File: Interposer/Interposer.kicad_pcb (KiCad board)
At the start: 2 copper layers, 55 x 52 mm, 34 parts, among them J7 Conn_01x14_MountingPin, Q3 2N7002, U13 AD40xxBRMZ, U14 LP5907MFX-1.8, U6 ADA4940-1xCP

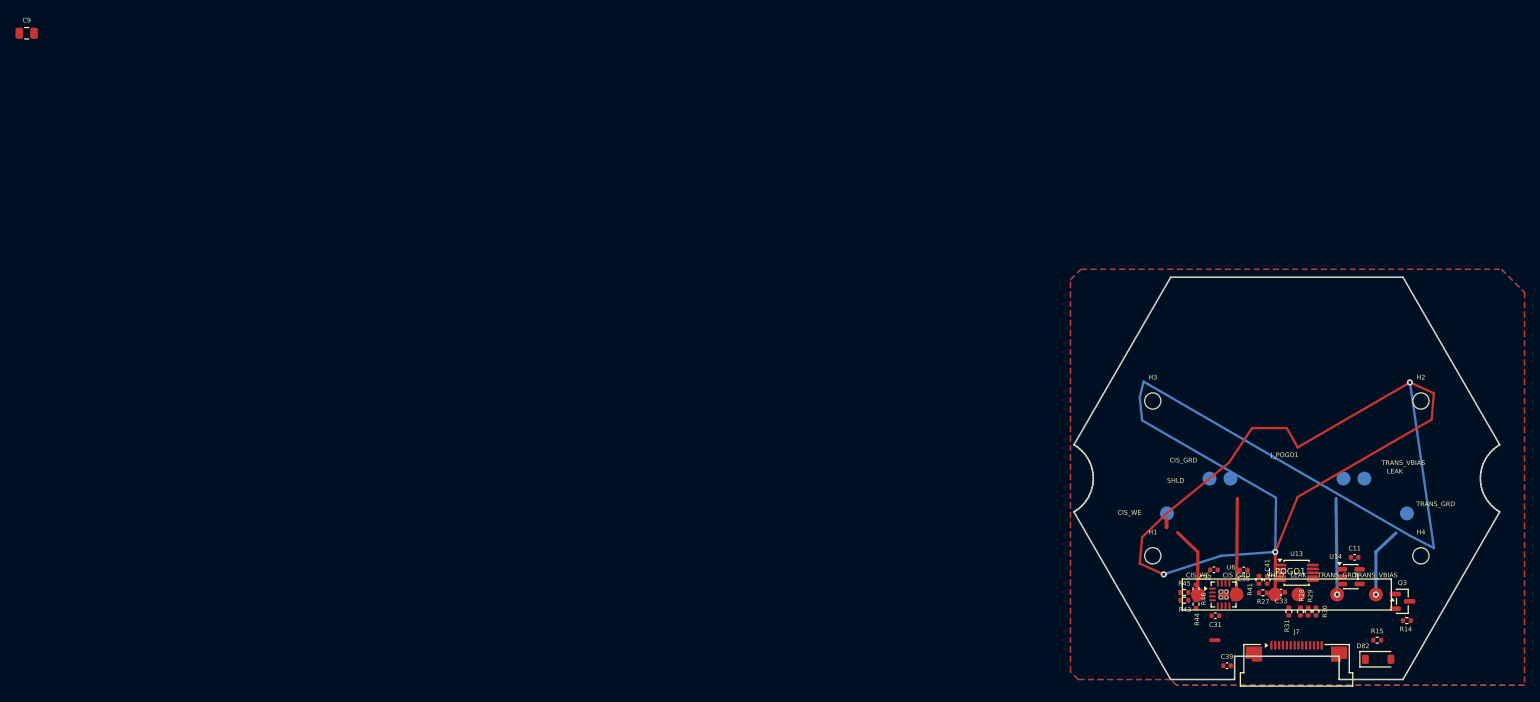
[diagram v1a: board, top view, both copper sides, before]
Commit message: fix(interposer): add missing H2-H4 holes and 12-pin pogo target array
Co-authored-by: google-labs-jules[bot] <161369871+google-labs-jules[bot]@users.noreply.github.com>
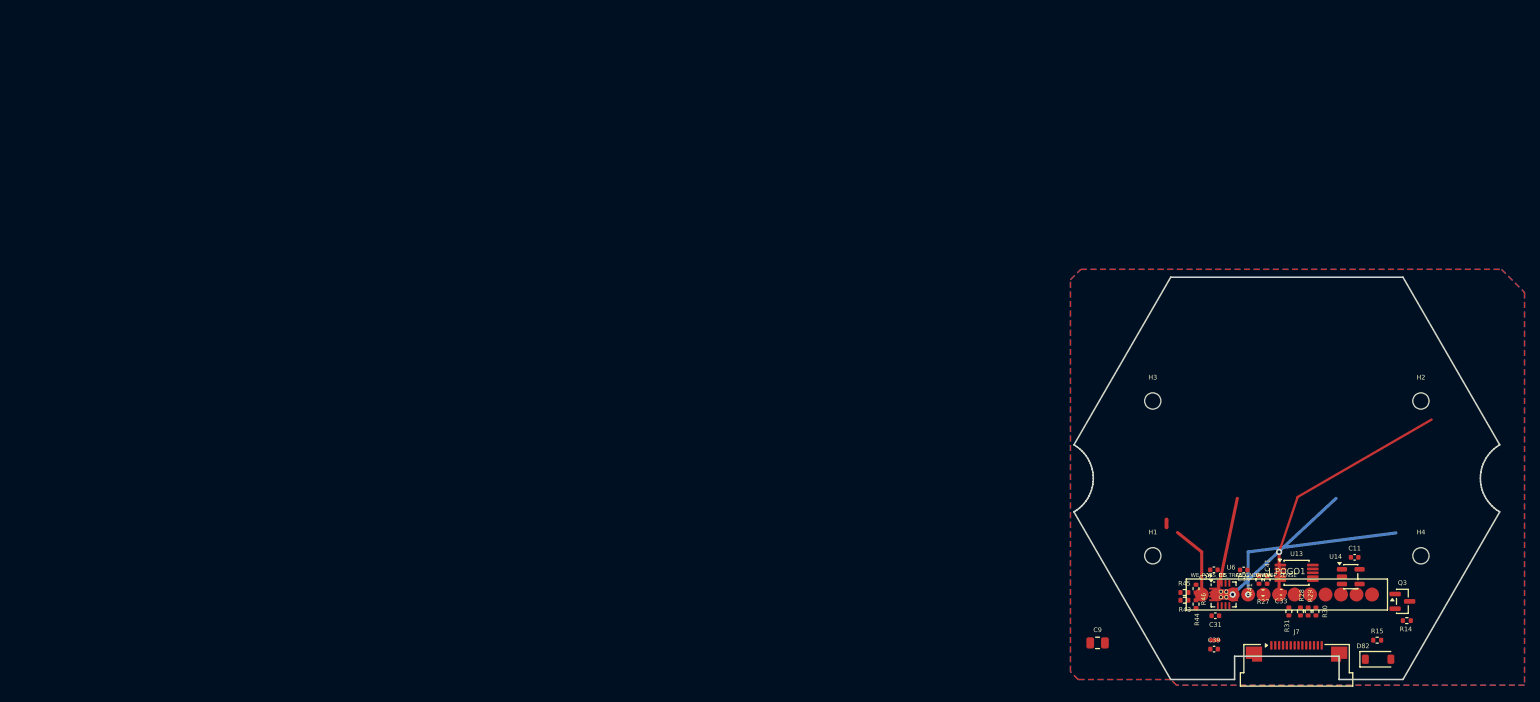
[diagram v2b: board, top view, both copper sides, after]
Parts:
- removed the J_POGO1 at (164.5, 58.5)
- moved C9 159.2 mm to (140.1, 79.8)
- moved C39 2.72 mm to (155.1, 80.5)
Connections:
- net /Signal_AMP renamed /Signal_Return
- J7 pad 10: VSSA -> VDDA
- J7 pad 12: VDDA -> VSSA
- J_POGO1 pad 1: >PORE_AMP -> WE_POS
- J_POGO1 pad 2: GUARD -> WS_CIS
- J_POGO1 pad 3: GNDA -> RE_TRANS
- J_POGO1 pad 4: WEEP_SENSE -> CE_GNDA
- J_POGO1 pad 5: GUARD_TRANS -> GNDA
- J_POGO1 pad 6: Vbias -> WEEP_SENSE
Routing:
- net WEEP_SENSE: track 202.8 -> 33.0 mm, vias 3 -> 1
- net CE_GNDA: track 9.07 -> 24.8 mm
- net RE_TRANS: track 12.4 -> 18.2 mm

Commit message: fix: Reconcile MR1 board stackup, BOM, interposer, and pore guidelines
Co-authored-by: google-labs-jules[bot] <161369871+google-labs-jules[bot]@users.noreply.github.com>
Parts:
- removed C11: 4.7u, Capacitor_SMD:C_0402_1005Metric
- removed C31, C32, C33, C39: 100nF, Capacitor_SMD:C_0402_1005Metric
- removed C35: 10u, Capacitor_SMD:C_0402_1005Metric
- removed C41: 1nF, Capacitor_SMD:C_0402_1005Metric
- removed C9: 100nF, Capacitor_SMD:C_0805_2012Metric
- removed D82: MBR0540, Diode_SMD:D_SOD-123
- removed J7: Conn_01x14_MountingPin, Connector_FFC-FPC:Amphenol_F32R-1A7x1-11014_1x14-1MP_P0.5mm_Horizontal
- removed NT7, NT8: NetTie_2, NetTie:NetTie-2_SMD_Pad0.5mm
- removed Q3: 2N7002, Package_TO_SOT_SMD:SOT-23
- removed R14, R15: 100k, Resistor_SMD:R_0402_1005Metric
- removed R27, R41: 27, Resistor_SMD:R_0402_1005Metric
- removed R28, R29, R30, R31: 49.9, Resistor_SMD:R_0402_1005Metric
- removed R43, R44, R45, R46: 499 (0.1%), Resistor_SMD:R_0402_1005Metric
- removed U13: AD40xxBRMZ, Package_SO:MSOP-10_3x3mm_P0.5mm
- removed U14: LP5907MFX-1.8, Package_TO_SOT_SMD:SOT-23-5
- removed U6: ADA4940-1xCP, Package_CSP:LFCSP-16-1EP_3x3mm_P0.5mm_EP1.3x1.3mm_ThermalVias

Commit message: feat: Add Path 2 wideband TIA channel for 200nm pores
Co-authored-by: google-labs-jules[bot] <161369871+google-labs-jules[bot]@users.noreply.github.com>
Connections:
- J_POGO1 pad 1: WE_POS -> CE_GNDA
- J_POGO1 pad 10: GUARD -> WS_CIS_WIDE
- J_POGO1 pad 11: GUARD -> GNDA
- J_POGO1 pad 12: GUARD -> WEEP_SENSE
- J_POGO1 pad 2: WS_CIS -> RE_TRANS
- J_POGO1 pad 3: RE_TRANS -> >PORE
- J_POGO1 pad 4: CE_GNDA -> GNDA
- J_POGO1 pad 5: GNDA -> GUARD
- J_POGO1 pad 6: WEEP_SENSE -> WS_CIS
- J_POGO1 pad 7: GUARD_TRANS -> GUARD
- J_POGO1 pad 8: GUARD -> GNDA
- J_POGO1 pad 9: GUARD -> GUARD_WIDE
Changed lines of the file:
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@@
 				(type "core")
 				(color "PTFE natural")
-				(thickness 0.71)
-				(material "PTFE")
+				(thickness 1.5)
+				(material "Rogers RO3003 / PTFE")
 				(epsilon_r 2.1)
 				(loss_tangent 0.0002)
@@
 		(fp_line (start 13.0 2.0) (end -13.0 2.0) (stroke (width 0.15) (type default)) (layer "F.SilkS"))
 		(fp_line (start -13.0 2.0) (end -13.0 -2.0) (stroke (width 0.15) (type default)) (layer "F.SilkS"))
-		(fp_text user "WE_POS" (at -11.0 -2.5 0) (layer "F.SilkS") (effects (font (size 0.5 0.5) (thickness 0.08))))
-		(fp_text user "WS_CIS" (at -9.0 -2.5 0) (layer "F.SilkS") (effects (font (size 0.5 0.5) (thickness 0.08))))
-		(fp_text user "RE_TRANS" (at -7.0 -2.5 0) (layer "F.SilkS") (effects (font (size 0.5 0.5) (thickness 0.08))))
-		(fp_text user "CE_GNDA" (at -5.0 -2.5 0) (layer "F.SilkS") (effects (font (size 0.5 0.5) (thickness 0.08))))
-		(fp_text user "GNDA" (at -3.0 -2.5 0) (layer "F.SilkS") (effects (font (size 0.5 0.5) (thickness 0.08))))
-		(fp_text user "WEEP_SENSE" (at -1.0 -2.5 0) (layer "F.SilkS") (effects (font (size 0.5 0.5) (thickness 0.08))))
-		(pad "1" smd circle (at -11.0 0) (size 1.8 1.8) (layers "F.Cu" "F.Mask") (clearance 0.4) (zone_connect 0) (net "WE_POS"))
-		(pad "2" smd circle (at -9.0 0) (size 1.8 1.8) (layers "F.Cu" "F.Mask") (clearance 0.4) (zone_connect 0) (net "WS_CIS"))
-		(pad "3" smd circle (at -7.0 0) (size 1.8 1.8) (layers "F.Cu" "F.Mask") (clearance 0.4) (zone_connect 0) (net "RE_TRANS"))
-		(pad "4" smd circle (at -5.0 0) (size 1.8 1.8) (layers "F.Cu" "F.Mask") (clearance 0.4) (zone_connect 0) (net "CE_GNDA"))
-		(pad "5" smd circle (at -3.0 0) (size 1.8 1.8) (layers "F.Cu" "F.Mask") (clearance 0.4) (zone_connect 0) (net "GNDA"))
-		(pad "6" smd circle (at -1.0 0) (size 1.8 1.8) (layers "F.Cu" "F.Mask") (clearance 0.4) (zone_connect 0) (net "WEEP_SENSE"))
-		(pad "7" smd circle (at 1.0 0) (size 1.8 1.8) (layers "F.Cu" "F.Mask") (clearance 0.4) (zone_connect 0) (net "GUARD_TRANS"))
-		(pad "8" smd circle (at 3.0 0) (size 1.8 1.8) (layers "F.Cu" "F.Mask") (clearance 0.4) (zone_connect 0) (net "GUARD"))
-		(pad "9" smd circle (at 5.0 0) (size 1.8 1.8) (layers "F.Cu" "F.Mask") (clearance 0.4) (zone_connect 0) (net "GUARD"))
-		(pad "10" smd circle (at 7.0 0) (size 1.8 1.8) (layers "F.Cu" "F.Mask") (clearance 0.4) (zone_connect 0) (net "GUARD"))
-		(pad "11" smd circle (at 9.0 0) (size 1.8 1.8) (layers "F.Cu" "F.Mask") (clearance 0.4) (zone_connect 0) (net "GUARD"))
-		(pad "12" smd circle (at 11.0 0) (size 1.8 1.8) (layers "F.Cu" "F.Mask") (clearance 0.4) (zone_connect 0) (net "GUARD"))
+		(fp_text user "CE_GNDA" (at -11.0 -2.5 0) (layer "F.SilkS") (uuid "uuid-1") (effects (font (size 0.5 0.5) (thickness 0.08))))
+		(fp_text user "RE_TRANS" (at -9.0 -2.5 0) (layer "F.SilkS") (uuid "uuid-2") (effects (font (size 0.5 0.5) (thickness 0.08))))
+		(fp_text user ">PORE" (at -7.0 -2.5 0) (layer "F.SilkS") (uuid "uuid-3") (effects (font (size 0.5 0.5) (thickness 0.08))))
+		(fp_text user "GNDA" (at -5.0 -2.5 0) (layer "F.SilkS") (uuid "uuid-4") (effects (font (size 0.5 0.5) (thickness 0.08))))
+		(fp_text user "GUARD" (at -3.0 -2.5 0) (layer "F.SilkS") (uuid "uuid-5") (effects (font (size 0.5 0.5) (thickness 0.08))))
+		(fp_text user "WS_CIS" (at -1.0 -2.5 0) (layer "F.SilkS") (uuid "uuid-6") (effects (font (size 0.5 0.5) (thickness 0.08))))
+		(fp_text user "GUARD" (at 1.0 -2.5 0) (layer "F.SilkS") (uuid "uuid-7") (effects (font (size 0.5 0.5) (thickness 0.08))))
+		(fp_text user "GNDA" (at 3.0 -2.5 0) (layer "F.SilkS") (uuid "uuid-8") (effects (font (size 0.5 0.5) (thickness 0.08))))
+		(fp_text user "GUARD_WIDE" (at 5.0 -2.5 0) (layer "F.SilkS") (uuid "uuid-9") (effects (font (size 0.5 0.5) (thickness 0.08))))
+		(fp_text user "WS_CIS_WIDE" (at 7.0 -2.5 0) (layer "F.SilkS") (uuid "uuid-10") (effects (font (size 0.5 0.5) (thickness 0.08))))
+		(fp_text user "GNDA" (at 9.0 -2.5 0) (layer "F.SilkS") (uuid "uuid-11") (effects (font (size 0.5 0.5) (thickness 0.08))))
+		(fp_text user "WEEP_SENSE" (at 11.0 -2.5 0) (layer "F.SilkS") (uuid "uuid-12") (effects (font (size 0.5 0.5) (thickness 0.08))))
+		(pad "1" smd circle (at -11.0 0) (size 1.8 1.8) (layers "F.Cu" "F.Mask") (clearance 0.4) (zone_connect 0) (net "CE_GNDA") (uuid "uuid-pad-1"))
+		(pad "2" smd circle (at -9.0 0) (size 1.8 1.8) (layers "F.Cu" "F.Mask") (clearance 0.4) (zone_connect 0) (net "RE_TRANS") (uuid "uuid-pad-2"))
+		(pad "3" smd circle (at -7.0 0) (size 1.8 1.8) (layers "F.Cu" "F.Mask") (clearance 0.4) (zone_connect 0) (net ">PORE") (uuid "uuid-pad-3"))
+		(pad "4" smd circle (at -5.0 0) (size 1.8 1.8) (layers "F.Cu" "F.Mask") (clearance 0.4) (zone_connect 0) (net "GNDA") (uuid "uuid-pad-4"))
+		(pad "5" smd circle (at -3.0 0) (size 1.8 1.8) (layers "F.Cu" "F.Mask") (clearance 0.4) (zone_connect 0) (net "GUARD") (uuid "uuid-pad-5"))
+		(pad "6" smd circle (at -1.0 0) (size 1.8 1.8) (layers "F.Cu" "F.Mask") (clearance 0.4) (zone_connect 0) (net "WS_CIS") (uuid "uuid-pad-6"))
+		(pad "7" smd circle (at 1.0 0) (size 1.8 1.8) (layers "F.Cu" "F.Mask") (clearance 0.4) (zone_connect 0) (net "GUARD") (uuid "uuid-pad-7"))
+		(pad "8" smd circle (at 3.0 0) (size 1.8 1.8) (layers "F.Cu" "F.Mask") (clearance 0.4) (zone_connect 0) (net "GNDA") (uuid "uuid-pad-8"))
+		(pad "9" smd circle (at 5.0 0) (size 1.8 1.8) (layers "F.Cu" "F.Mask") (clearance 0.4) (zone_connect 0) (net "GUARD_WIDE") (uuid "uuid-pad-9"))
+		(pad "10" smd circle (at 7.0 0) (size 1.8 1.8) (layers "F.Cu" "F.Mask") (clearance 0.4) (zone_connect 0) (net "WS_CIS_WIDE") (uuid "uuid-pad-10"))
+		(pad "11" smd circle (at 9.0 0) (size 1.8 1.8) (layers "F.Cu" "F.Mask") (clearance 0.4) (zone_connect 0) (net "GNDA") (uuid "uuid-pad-11"))
+		(pad "12" smd circle (at 11.0 0) (size 1.8 1.8) (layers "F.Cu" "F.Mask") (clearance 0.4) (zone_connect 0) (net "WEEP_SENSE") (uuid "uuid-pad-12"))
 	)
 	(gr_line
@@
 	)
 	(embedded_fonts no)
+	(gr_poly
+		(pts
+			(xy 159.0 56.0) (xy 171.0 56.0) (xy 171.0 63.0) (xy 159.0 63.0)
+		)
+		(stroke
+			(width 0.1)
+			(type solid)
+		)
+		(fill yes)
+		(layer "F.Mask")
+	)
+	(gr_poly
+		(pts
+			(xy 159.0 56.0) (xy 171.0 56.0) (xy 171.0 63.0) (xy 159.0 63.0)
+		)
+		(stroke
+			(width 0.1)
+			(type solid)
+		)
+		(fill yes)
+		(layer "B.Mask")
+	)
 	(segment (start 153.5 73.5) (end 153.5 68) (width 0.4) (layer "F.Cu") (net "WE_POS"))
 	(segment (start 153.5 68) (end 150.37866 65.488975) (width 0.4) (layer "F.Cu") (net "WE_POS"))

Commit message: adding new symbols
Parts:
- added J_POGO2: PogoPin_Target_6Pin_Trans, footprints:PogoPin_Target_6Pin_Trans, F.Cu at (164.5, 73.5)
- J_POGO1: value PogoPin_Target_12Pin_Distributed -> PogoPin_Target_6Pin_Cis; footprint footprints:PogoPin_Target_12Pin_Distributed -> footprints:PogoPin_Target_6Pin_Cis
- moved J_POGO1 30.0 mm to (164.5, 43.5)
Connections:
- net RE_TRANS renamed >PORE_AMP
- J_POGO1 pad 1: CE_GNDA -> GNDA
- J_POGO1 pad 3: >PORE -> GNDA
- J_POGO1 pad 4: GNDA -> GUARD
- J_POGO1 pad 5: GUARD -> GNDA
- J_POGO1 pad 6: WS_CIS -> WEEP_SENSE
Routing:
- net WEEP_SENSE: track 33.0 -> 0.00 mm, vias 1 -> 0
- net CE_GNDA: track 24.8 -> 0.00 mm, vias 1 -> 0
- net >PORE_AMP: track 18.2 -> 0.00 mm, vias 1 -> 0
- net GUARD: track 0.00 -> 15.1 mm
- net WS_CIS: track 12.7 -> 0.00 mm
- net WE_POS: track 9.51 -> 0.00 mm
- net GNDA: track 0.00 -> 3.55 mm
- net GUARD_WIDE: track 0.00 -> 1.55 mm

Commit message: Tune torque cap flexure arms (tongs) for pogo pin and seal compression
Adjust Torque_Cap_Outer 6 cantilever flexure arms in src/torque_cap.py
from a stiff 4.0 mm block to a compliant living hinge thickness of 1.8 mm
(tuned for 4 perimeter passes of 0.45 mm nozzle PETG) with 2.5 mm root
fillets and optimized pawl tip engagement. This prevents over-tightening
against the inner threaded insert while delivering the required clamping
force for 12 pogo pins (~9.6 N) and silicone gasket compression.

Document the physical relation in src/constants.py and verify via
simulations/flexure_living_hinge_fea.py and tests/test_geometry.py.

Co-authored-by: google-labs-jules[bot] <161369871+google-labs-jules[bot]@users.noreply.github.com>
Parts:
- removed J_POGO2: PogoPin_Target_6Pin_Trans, footprints:PogoPin_Target_6Pin_Trans
- J_POGO1: value PogoPin_Target_6Pin_Cis -> PogoPin_Target_12Pin_Distributed; footprint footprints:PogoPin_Target_6Pin_Cis -> footprints:PogoPin_Target_12Pin_Distributed
- moved J_POGO1 30.0 mm to (164.5, 73.5)
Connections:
- J_POGO1 pad 1: GNDA -> CE_GNDA
- J_POGO1 pad 2: >PORE_AMP -> RE_TRANS
- J_POGO1 pad 3: GNDA -> >PORE
- J_POGO1 pad 4: GUARD -> GNDA
- J_POGO1 pad 5: GNDA -> GUARD
- J_POGO1 pad 6: WEEP_SENSE -> WS_CIS
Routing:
- net WEEP_SENSE: track 0.00 -> 33.0 mm, vias 0 -> 1
- net CE_GNDA: track 0.00 -> 24.8 mm, vias 0 -> 1
- net RE_TRANS: track 0.00 -> 18.2 mm, vias 0 -> 1
- net GUARD: track 15.1 -> 0.00 mm
- net WS_CIS: track 0.00 -> 12.7 mm
- net WE_POS: track 0.00 -> 9.51 mm
- net GNDA: track 3.55 -> 0.00 mm
- net GUARD_WIDE: track 1.55 -> 0.00 mm
